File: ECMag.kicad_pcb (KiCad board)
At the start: 2 copper layers, 110.5 x 59.7 mm, 48 parts, among them J1 Cn_01x12, J2 Cn_01x05, J3 Cn_01x04, J4 USB_B, J5 Barrel_Jack_SW, J6 Cn_01x04, K1 Switch, K2 Switch, K3 Switch, K4 Switch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

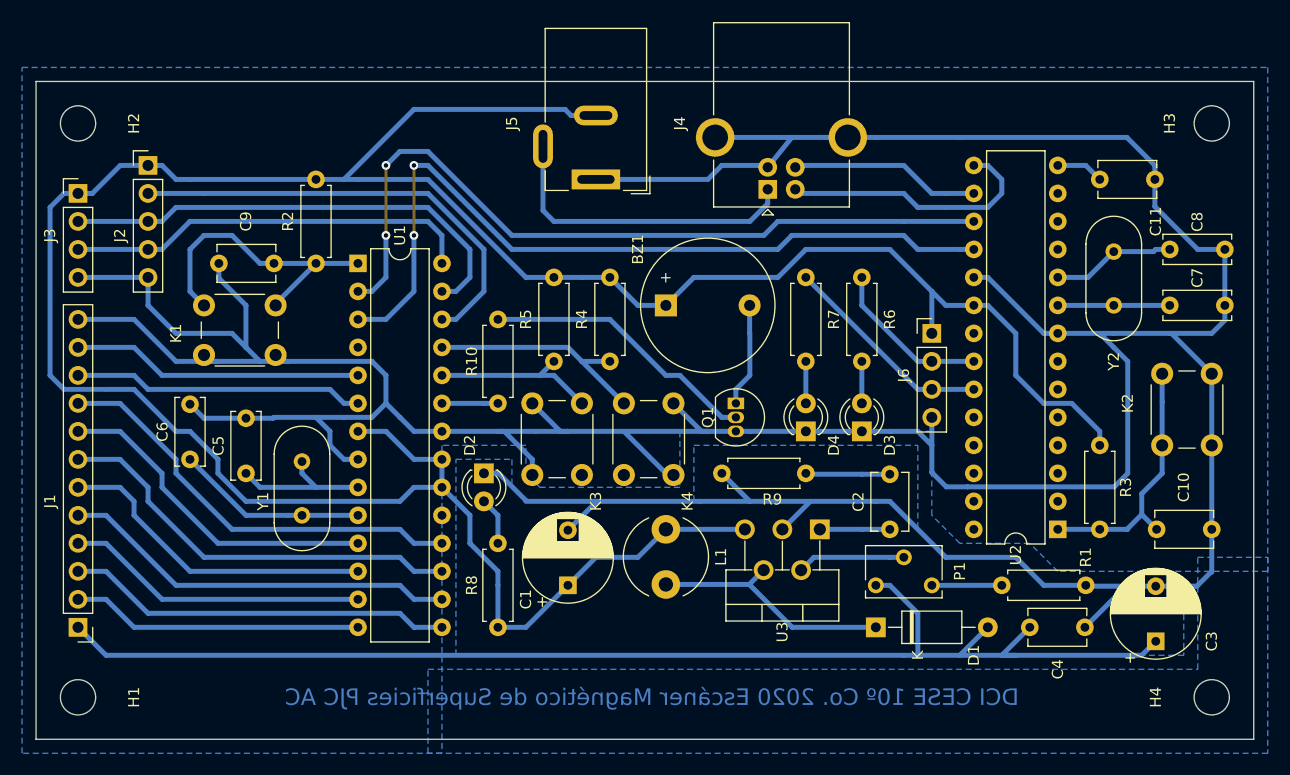
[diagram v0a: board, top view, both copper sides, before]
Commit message: Agregadas las imagenes 3D del power jack y del USB B, corregidas esquinas del pcb, agregados fiduciarios, parametros del circuito, grilla, datos del fabricante, dimensiones del pcb, datos de serigrafía, cambiada la licencia por la de BSD Modificada
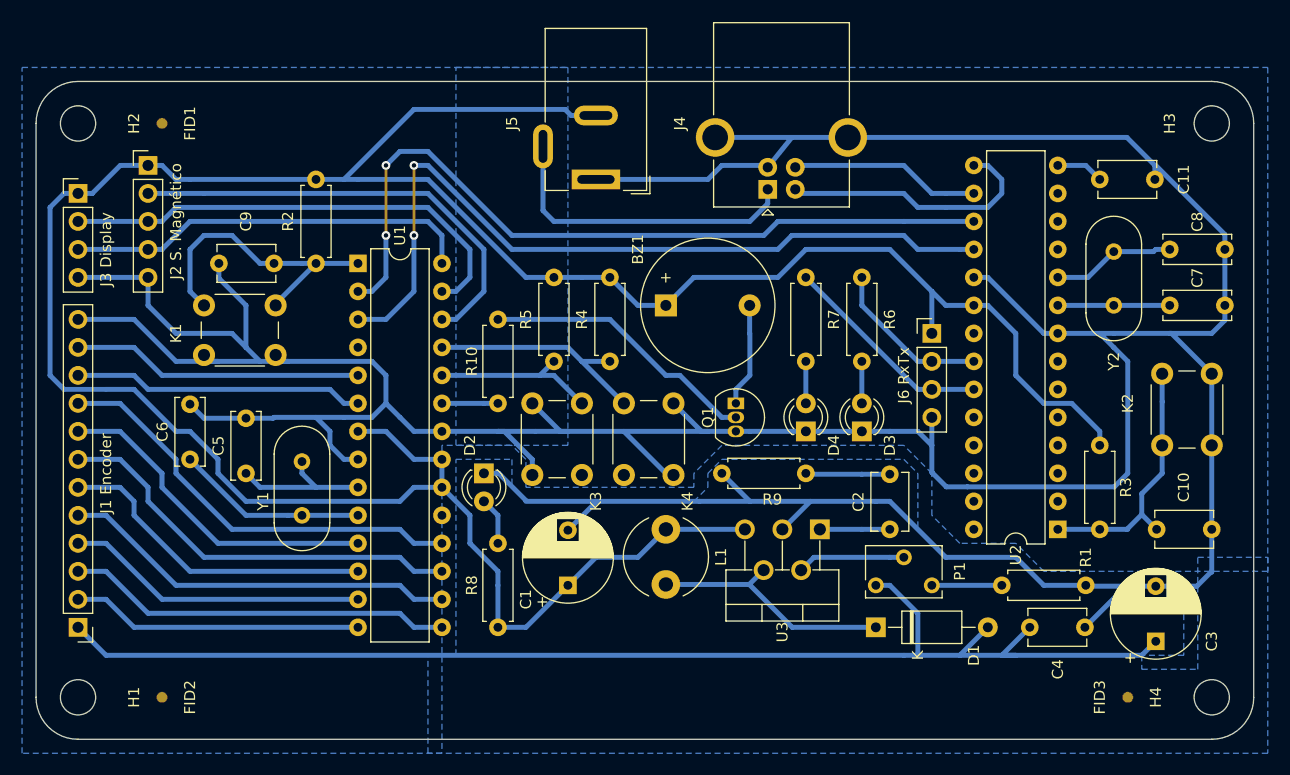
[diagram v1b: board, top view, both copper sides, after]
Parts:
- removed J1: Cn_01x12, Connector_PinHeader_2.54mm:PinHeader_1x12_P2.54mm_Vertical
- removed J2: Cn_01x05, Connector_PinHeader_2.54mm:PinHeader_1x05_P2.54mm_Vertical
- removed J3, J6: Cn_01x04, Connector_PinHeader_2.54mm:PinHeader_1x04_P2.54mm_Vertical
- added FID1: Fiducial, Fiducial:Fiducial_1mm_Mask2mm, F.Cu at (104.1, 74.9)
- added FID2: Fiducial, Fiducial:Fiducial_1mm_Mask2mm, F.Cu at (104.1, 127.0)
- added FID3: Fiducial, Fiducial:Fiducial_1mm_Mask2mm, F.Cu at (191.8, 127.0)
- added J1 Encoder: Conn_01x12, Connector_PinHeader_2.54mm:PinHeader_1x12_P2.54mm_Vertical, F.Cu at (96.5, 120.7)
- added J2 S. Magnético: Conn_01x05, Connector_PinHeader_2.54mm:PinHeader_1x05_P2.54mm_Vertical, F.Cu at (102.9, 78.7)
- added J3 Display: Conn_01x04, Connector_PinHeader_2.54mm:PinHeader_1x04_P2.54mm_Vertical, F.Cu at (96.5, 81.3)
- added J6 RxTx: Conn_01x04, Connector_PinHeader_2.54mm:PinHeader_1x04_P2.54mm_Vertical, F.Cu at (174.0, 94.0)
- K1, K2, K3, K4: value Switch -> Tactil Switch B3F NA
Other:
- outline, holes or cut-outs redrawn
- board text added: "CESE 10º Cohorte Fecha: 06/2020"
- board text added: "Estándares de fabricación MEYER SA Diámetro de agujero 16 (0,40 mm) Diámetro de pad o vía 28 (0,70 mm) Ancho de traza 5 (0,125 mm) Separación entre trazas 5 (0,125 mm) Separación entre traza y pad/vía 5 (0,125 mm) Distancia de cobre a borde 12 (0,30 mm) Antisoldante 2 (0.05 mm) Altura - trazo de letras 30 - 5"
- board text added: "Grilla 1,270 mm (50,00 mils) Diametro de pad o vía 0,80 mm Ancho de traza 0.450 mm Separación entre trazas 0,20 mm Separación entre traza y pad/vía 0.20 mm Cobre de 2 Oz (0,07 mm) Sustrato FR4 1,60 mm Terminación ENIG Leyendas en blanco Máscara antisoldante en verde"
- board text added: "Nombre: EcMag Autor: Pablo Alonso Castillo"
- board text added: "Version: 1.0 Rev: 1"
- board text removed: "DCI CESE 10º Co. 2020 Escáner Magnético de Superficies PJC AC"
